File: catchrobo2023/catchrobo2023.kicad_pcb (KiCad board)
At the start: 2 copper layers, 72 x 47 mm, 38 parts, among them J1 Conn_01x03_Male, J2 Conn_01x03_Male, J3 Conn_01x03_Male, J4 Conn_01x02_Male, J5 Conn_01x02_Male, J6 Conn_01x02_Male, J7 Conn_01x02_Male, J8 Conn_01x02_Male, Q1 AO3401A, SW1 SW_SPDT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

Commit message: 部品配置一旦終わり
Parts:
- U4, U5, U6, U7: footprint Connector_JST:JST_XH_B4B-XH-AM_1x04_P2.50mm_Vertical -> Connector_PinHeader_2.54mm:PinHeader_1x04_P2.54mm_Vertical
- moved J5 114.1 mm to (117.8, 117.0), turned to 180 degrees
- moved J8 86.9 mm to (128.8, 117.0), turned to 180 degrees
- moved U11 50.5 mm to (107.0, 117.0), turned to 180 degrees
- moved R9 44.6 mm to (140.0, 113.5), turned to -90 degrees
- moved R5 41.1 mm to (147.5, 113.7), turned to 90 degrees
- moved R4 37.3 mm to (147.5, 107.5), turned to 90 degrees
- moved SW2 36.4 mm to (147.3, 87.8), turned to 180 degrees
- moved R8 33.9 mm to (140.0, 107.5), turned to -90 degrees
- moved R3 29.9 mm to (147.5, 101.7), turned to 90 degrees
- moved R7 29.0 mm to (140.0, 101.5), turned to -90 degrees
- moved U8 27.5 mm to (125.5, 100.0), turned to 180 degrees
- moved R6 24.7 mm to (140.0, 95.5), turned to -90 degrees
- moved U7 24.0 mm to (147.5, 110.5), turned to -90 degrees
- moved U4 18.0 mm to (147.5, 92.5), turned to -90 degrees
- moved R2 15.1 mm to (147.5, 95.7), turned to 90 degrees
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
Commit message: 部品配置完了！
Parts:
- moved D3 9.50 mm to (107.0, 75.5)
- moved D2 8.62 mm to (121.5, 82.2)
- moved R1 8.50 mm to (116.5, 86.0)
- moved R10 8.00 mm to (113.5, 86.0)
- moved U8 4.61 mm to (130.0, 99.0), turned to 0 degrees
- moved J1 4.00 mm to (92.5, 118.0)
- moved J2 4.00 mm to (97.0, 118.0)
- moved J3 4.00 mm to (101.5, 118.0)
- moved C2 4.00 mm to (84.0, 86.5)
- moved J5 4.00 mm to (121.8, 117.0)
- moved J8 4.00 mm to (132.8, 117.0)
- moved U11 4.00 mm to (111.0, 117.0)
- moved U2 2.92 mm to (111.0, 99.0)
- moved SW2 1.12 mm to (148.3, 87.3)
- moved R11 1.01 mm to (111.5, 80.8)
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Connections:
- U2 pad 21: /MultiC -> unconnected-(U2-Pad21)
- U8 pad 1: /Sensor0 -> unconnected-(U8-Pad1)
- U8 pad 12: unconnected-(U8-Pad12) -> /Sensor3
- U8 pad 13: unconnected-(U8-Pad13) -> /Sensor2
- U8 pad 14: unconnected-(U8-Pad14) -> /Sensor1
- U8 pad 15: unconnected-(U8-Pad15) -> /Sensor0
- U8 pad 2: /Sensor1 -> unconnected-(U8-Pad2)
- U8 pad 4: /Sensor2 -> unconnected-(U8-Pad4)
- U8 pad 5: /Sensor3 -> unconnected-(U8-Pad5)
- U8 pad 9: /MultiC -> unconnected-(U8-Pad9)
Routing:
- net +5V: track 0.00 -> 104.3 mm
- net +3.3V: track 0.00 -> 61.3 mm
- net /Stopper: track 0.00 -> 29.4 mm, vias 0 -> 1
- net /Sensor: track 0.00 -> 28.1 mm
- net /DIPSW3: track 0.00 -> 25.1 mm
- net /DIPSW2: track 0.00 -> 21.6 mm
- net /Sensor3: track 0.00 -> 18.3 mm
- net /DIPSW1: track 0.00 -> 17.9 mm
- net /Speaker: track 0.00 -> 17.7 mm
- net /Sensor0: track 0.00 -> 17.1 mm
- net /STEP1: track 0.00 -> 15.8 mm
- net /DIR1: track 0.00 -> 15.8 mm
- net /DIR2: track 0.00 -> 14.6 mm
- net GND: track 0.00 -> 14.5 mm
- net /DIPSW0: track 0.00 -> 14.3 mm
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- added copper zone on F.Cu, net +5V
- added copper zone on F.Cu, net +7.5V
- added copper zone on F.Cu, net +BATT
- added copper zone on F.Cu, net Net-(D3-Pad2)
- added copper zone on F.Cu, net Net-(J4-Pad1)

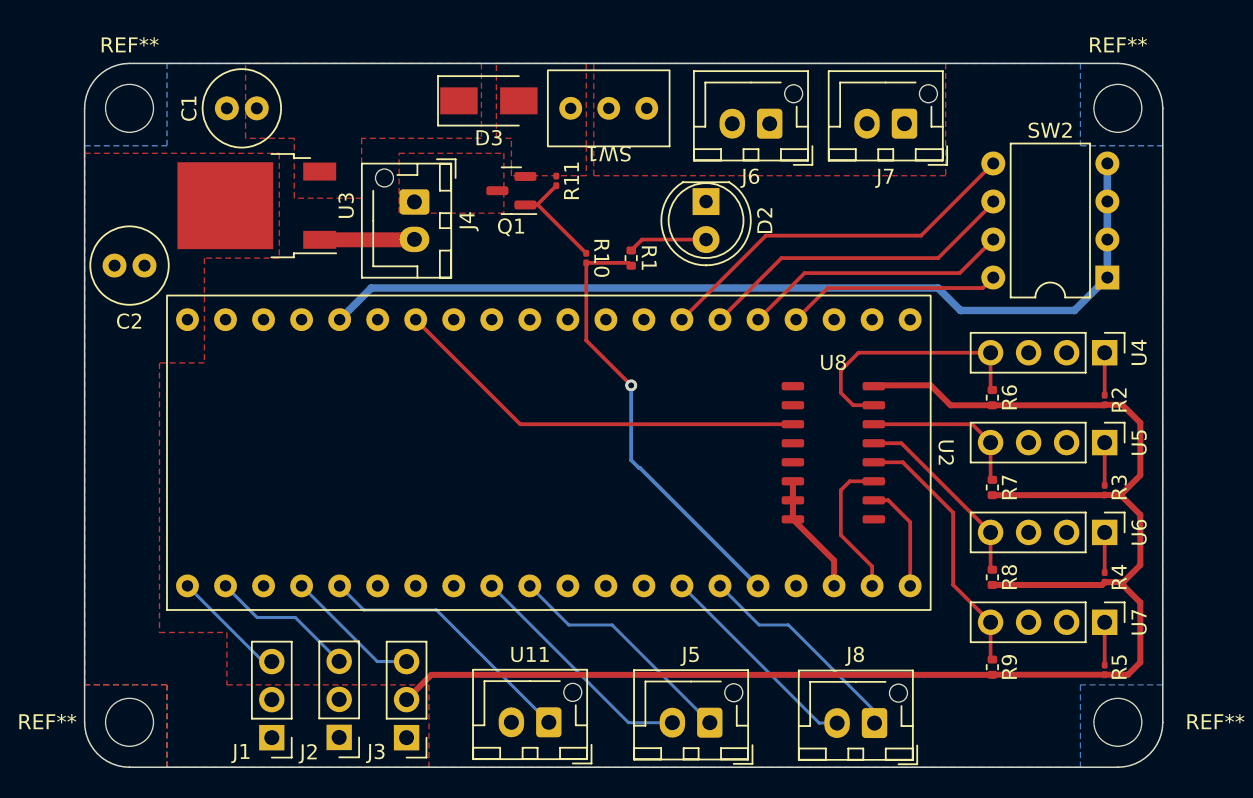
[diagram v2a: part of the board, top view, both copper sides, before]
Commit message: 基板上のシルクを整備（ピン番号の表記など）
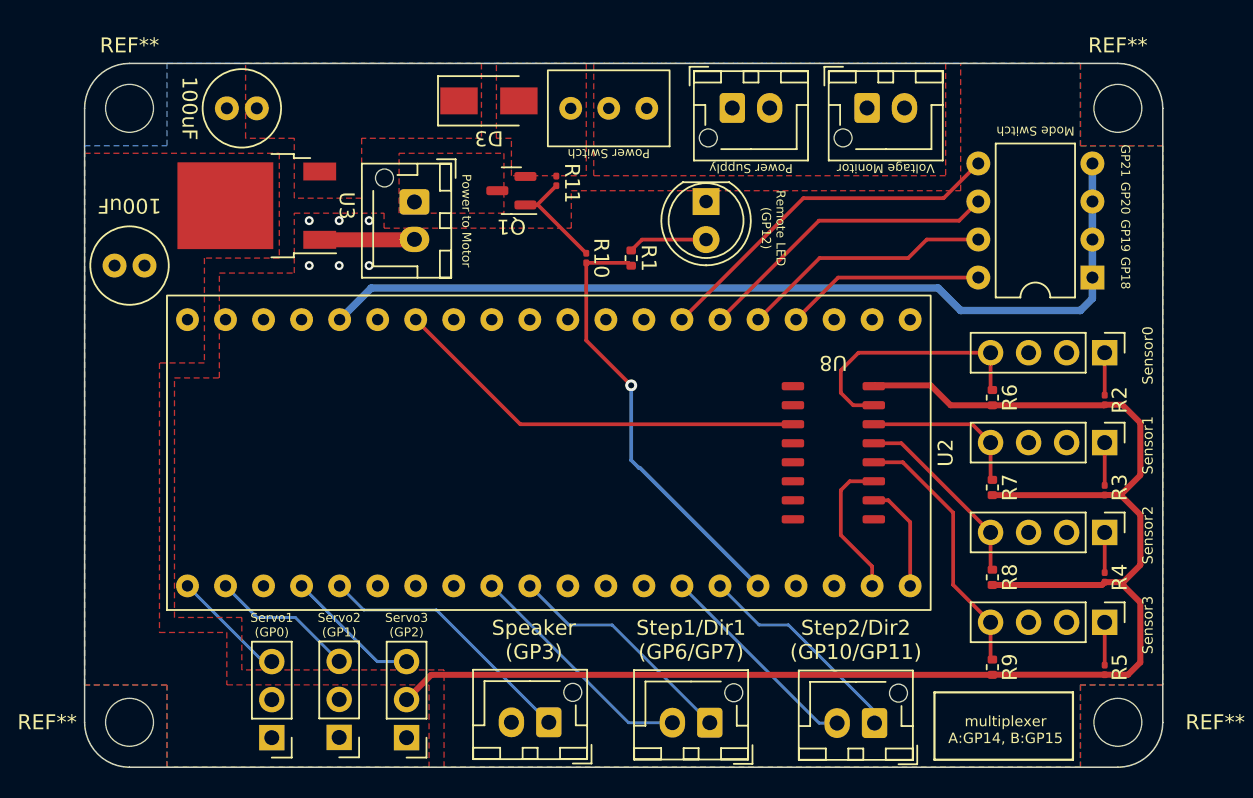
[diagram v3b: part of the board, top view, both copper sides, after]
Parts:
- moved J6 2.71 mm to (123.2, 76.0), turned to 0 degrees
- moved J7 2.71 mm to (132.2, 76.0), turned to 0 degrees
- moved SW2 1.00 mm to (147.3, 87.3)
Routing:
- net GND: track 14.5 -> 6.34 mm, vias 0 -> 6
- net /DIPSW2: track 21.6 -> 20.5 mm
- net /DIPSW3: track 25.1 -> 24.1 mm
- net /DIPSW1: track 17.9 -> 16.9 mm
- net /DIPSW0: track 14.3 -> 13.3 mm
- added copper zone on F.Cu, net GND
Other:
- board text added: "100uF"
- board text added: "GP18"
- board text added: "GP19"
- board text added: "GP20"
- board text added: "GP21"
- board text added: "Mode Switch"
- board text added: "Power Supply"
- board text added: "Power Switch"
- board text added: "Power to Motor"
- board text added: "Remote LED (GP12)"
- board text added: "Sensor0"
- board text added: "Sensor1"
- board text added: "Sensor2"
- board text added: "Sensor3"
- board text added: "Servo1 (GP0)"
- board text added: "Servo2 (GP1)"
- board text added: "Servo3 (GP2)"
- board text added: "Speaker (GP3)"
- board text added: "Step1/Dir1 (GP6/GP7)"
- board text added: "Step2/Dir2 (GP10/GP11)"
- board text added: "Voltage Monitor"
- board text added: "multiplexer A:GP14, B:GP15"
